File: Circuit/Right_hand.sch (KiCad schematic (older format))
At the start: 2 parts, among them P5 LW_ADC, P6 RW_ADC

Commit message: 実態配線図書き始め
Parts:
- P5, P6: footprint (none) -> YASU:XA_3Pin
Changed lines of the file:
@@
 LIBS:contrib
 LIBS:valves
+LIBS:YASU
 LIBS:device
+LIBS:robocon_sch
 LIBS:rhand_controller-cache
 EELAYER 25 0
@@
 F 0 "P6" H 4400 4300 50  0000 C CNN
 F 1 "RW_ADC" V 4500 4100 50  0000 C CNN
-F 2 "" H 4400 4100 50  0001 C CNN
+F 2 "YASU:XA_3Pin" H 4400 4100 50  0001 C CNN
 F 3 "" H 4400 4100 50  0000 C CNN
 	1    4400 4100
@@
 F 0 "P5" H 4400 3550 50  0000 C CNN
 F 1 "LW_ADC" V 4500 3350 50  0000 C CNN
-F 2 "" H 4400 3350 50  0001 C CNN
+F 2 "YASU:XA_3Pin" H 4400 3350 50  0001 C CNN
 F 3 "" H 4400 3350 50  0000 C CNN
 	1    4400 3350

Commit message: 部品割り付けの完了
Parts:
- renumbered P5 to P7, P6 to P8
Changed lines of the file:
@@
 LIBS:YASU
 LIBS:device
-LIBS:robocon_sch
 LIBS:rhand_controller-cache
 EELAYER 25 0
@@
 $EndDescr
 $Comp
-L CONN_01X03 P6
+L CONN_01X03 P8
 U 1 1 593D9ECA
 P 4400 4100
-F 0 "P6" H 4400 4300 50  0000 C CNN
+F 0 "P8" H 4400 4300 50  0000 C CNN
 F 1 "RW_ADC" V 4500 4100 50  0000 C CNN
 F 2 "YASU:XA_3Pin" H 4400 4100 50  0001 C CNN
@@
 $EndComp
 $Comp
-L CONN_01X03 P5
+L CONN_01X03 P7
 U 1 1 593D9EDE
 P 4400 3350
-F 0 "P5" H 4400 3550 50  0000 C CNN
+F 0 "P7" H 4400 3550 50  0000 C CNN
 F 1 "LW_ADC" V 4500 3350 50  0000 C CNN
 F 2 "YASU:XA_3Pin" H 4400 3350 50  0001 C CNN

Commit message: 部品を基板上へ適当に配置
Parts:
- P7: value LW_ADC -> JoyX
- P8: value RW_ADC -> JoyY
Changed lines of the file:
@@
 P 4400 4100
 F 0 "P8" H 4400 4300 50  0000 C CNN
-F 1 "RW_ADC" V 4500 4100 50  0000 C CNN
+F 1 "JoyY" V 4500 4100 50  0000 C CNN
 F 2 "YASU:XA_3Pin" H 4400 4100 50  0001 C CNN
 F 3 "" H 4400 4100 50  0000 C CNN
@@
 $EndComp
 $Comp
-L GND #PWR034
+L GND #PWR036
 U 1 1 593D9ED1
 P 4600 4250
-F 0 "#PWR034" H 4600 4000 50  0001 C CNN
+F 0 "#PWR036" H 4600 4000 50  0001 C CNN
 F 1 "GND" H 4600 4100 50  0000 C CNN
 F 2 "" H 4600 4250 50  0000 C CNN
@@
 $EndComp
 $Comp
-L +3.3V #PWR035
+L +3.3V #PWR037
 U 1 1 593D9ED7
 P 4600 3950
-F 0 "#PWR035" H 4600 3800 50  0001 C CNN
+F 0 "#PWR037" H 4600 3800 50  0001 C CNN
 F 1 "+3.3V" H 4600 4090 50  0000 C CNN
 F 2 "" H 4600 3950 50  0000 C CNN
@@
 P 4400 3350
 F 0 "P7" H 4400 3550 50  0000 C CNN
-F 1 "LW_ADC" V 4500 3350 50  0000 C CNN
+F 1 "JoyX" V 4500 3350 50  0000 C CNN
 F 2 "YASU:XA_3Pin" H 4400 3350 50  0001 C CNN
 F 3 "" H 4400 3350 50  0000 C CNN
@@
 $EndComp
 $Comp
-L GND #PWR036
+L GND #PWR038
 U 1 1 593D9EE5
 P 4600 3500
-F 0 "#PWR036" H 4600 3250 50  0001 C CNN
+F 0 "#PWR038" H 4600 3250 50  0001 C CNN
 F 1 "GND" H 4600 3350 50  0000 C CNN
 F 2 "" H 4600 3500 50  0000 C CNN
@@
 $EndComp
 $Comp
-L +3.3V #PWR037
+L +3.3V #PWR039
 U 1 1 593D9EEB
 P 4600 3200
-F 0 "#PWR037" H 4600 3050 50  0001 C CNN
+F 0 "#PWR039" H 4600 3050 50  0001 C CNN
 F 1 "+3.3V" H 4600 3340 50  0000 C CNN
 F 2 "" H 4600 3200 50  0000 C CNN

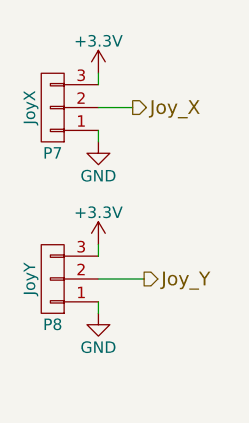
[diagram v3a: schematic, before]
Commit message: ADCのピン配置修正と配線引きはじめ
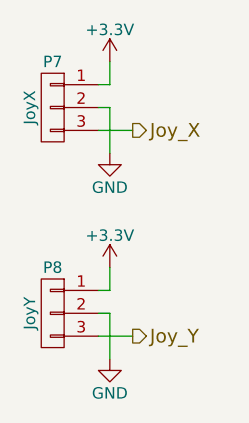
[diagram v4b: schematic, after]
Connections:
- net +3V3: now also P7.1 (P1), P8.1 (P1); no longer P7.3 (P3), P8.3 (P3)
- net GND: now also P7.2 (P2), P8.2 (P2); no longer P7.1 (P1), P8.1 (P1)
- net Joy_X: now also P7.3 (P3); no longer P7.2 (P2)
- net Joy_Y: now also P8.3 (P3); no longer P8.2 (P2)
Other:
- moved on the sheet: P8
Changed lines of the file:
@@
 LIBS:contrib
 LIBS:valves
-LIBS:YASU
 LIBS:device
+LIBS:robocon_sch
 LIBS:rhand_controller-cache
 EELAYER 25 0
@@
 L CONN_01X03 P8
 U 1 1 593D9ECA
-P 4400 4100
-F 0 "P8" H 4400 4300 50  0000 C CNN
-F 1 "JoyY" V 4500 4100 50  0000 C CNN
-F 2 "YASU:XA_3Pin" H 4400 4100 50  0001 C CNN
-F 3 "" H 4400 4100 50  0000 C CNN
-	1    4400 4100
-	-1   0    0    1
+P 4400 4250
+F 0 "P8" H 4400 4450 50  0000 C CNN
+F 1 "JoyY" V 4500 4250 50  0000 C CNN
+F 2 "YASU:XA_3Pin" H 4400 4250 50  0001 C CNN
+F 3 "" H 4400 4250 50  0000 C CNN
+	1    4400 4250
+	-1   0    0    -1
 $EndComp
 $Comp
 L GND #PWR036
 U 1 1 593D9ED1
-P 4600 4250
-F 0 "#PWR036" H 4600 4000 50  0001 C CNN
-F 1 "GND" H 4600 4100 50  0000 C CNN
-F 2 "" H 4600 4250 50  0000 C CNN
-F 3 "" H 4600 4250 50  0000 C CNN
-	1    4600 4250
+P 4650 4450
+F 0 "#PWR036" H 4650 4200 50  0001 C CNN
+F 1 "GND" H 4650 4300 50  0000 C CNN
+F 2 "" H 4650 4450 50  0000 C CNN
+F 3 "" H 4650 4450 50  0000 C CNN
+	1    4650 4450
 	1    0    0    -1
 $EndComp
@@
 L +3.3V #PWR037
 U 1 1 593D9ED7
-P 4600 3950
-F 0 "#PWR037" H 4600 3800 50  0001 C CNN
-F 1 "+3.3V" H 4600 4090 50  0000 C CNN
-F 2 "" H 4600 3950 50  0000 C CNN
-F 3 "" H 4600 3950 50  0000 C CNN
-	1    4600 3950
+P 4650 4050
+F 0 "#PWR037" H 4650 3900 50  0001 C CNN
+F 1 "+3.3V" H 4650 4190 50  0000 C CNN
+F 2 "" H 4650 4050 50  0000 C CNN
+F 3 "" H 4650 4050 50  0000 C CNN
+	1    4650 4050
 	1    0    0    -1
 $EndComp
@@
 F 3 "" H 4400 3350 50  0000 C CNN
 	1    4400 3350
-	-1   0    0    1
+	-1   0    0    -1
 $EndComp
 $Comp
 L GND #PWR038
 U 1 1 593D9EE5
-P 4600 3500
-F 0 "#PWR038" H 4600 3250 50  0001 C CNN
-F 1 "GND" H 4600 3350 50  0000 C CNN
-F 2 "" H 4600 3500 50  0000 C CNN
-F 3 "" H 4600 3500 50  0000 C CNN
-	1    4600 3500
+P 4650 3550
+F 0 "#PWR038" H 4650 3300 50  0001 C CNN
+F 1 "GND" H 4650 3400 50  0000 C CNN
+F 2 "" H 4650 3550 50  0000 C CNN
+F 3 "" H 4650 3550 50  0000 C CNN
+	1    4650 3550
 	1    0    0    -1
 $EndComp
@@
 L +3.3V #PWR039
 U 1 1 593D9EEB
-P 4600 3200
-F 0 "#PWR039" H 4600 3050 50  0001 C CNN
-F 1 "+3.3V" H 4600 3340 50  0000 C CNN
-F 2 "" H 4600 3200 50  0000 C CNN
-F 3 "" H 4600 3200 50  0000 C CNN
-	1    4600 3200
+P 4650 3150
+F 0 "#PWR039" H 4650 3000 50  0001 C CNN
+F 1 "+3.3V" H 4650 3290 50  0000 C CNN
+F 2 "" H 4650 3150 50  0000 C CNN
+F 3 "" H 4650 3150 50  0000 C CNN
+	1    4650 3150
 	1    0    0    -1
 $EndComp
 Wire Wire Line
-	4600 4200 4600 4250
+	4650 4250 4650 4450
 Wire Wire Line
-	4600 4000 4600 3950
+	4650 4150 4650 4050
+Text HLabel 4750 3450 2    60   Output ~ 0
+Joy_X
+Text HLabel 4750 4350 2    60   Output ~ 0
+Joy_Y
 Wire Wire Line
-	4600 4100 4800 4100
+	4600 3450 4750 3450
 Wire Wire Line
-	4600 3450 4600 3500
+	4600 3350 4650 3350
 Wire Wire Line
-	4600 3250 4600 3200
+	4650 3350 4650 3550
 Wire Wire Line
-	4600 3350 4750 3350
-Text HLabel 4750 3350 2    60   Output ~ 0
-Joy_X
-Text HLabel 4800 4100 2    60   Output ~ 0
-Joy_Y
+	4600 3250 4650 3250
+Wire Wire Line
+	4650 3250 4650 3150
+Wire Wire Line
+	4600 4150 4650 4150
+Wire Wire Line
+	4600 4250 4650 4250
+Wire Wire Line
+	4600 4350 4750 4350
 $EndSCHEMATC
